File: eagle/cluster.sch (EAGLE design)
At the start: 12 parts, among them J1 B7B-ZR_(LF)(SN)

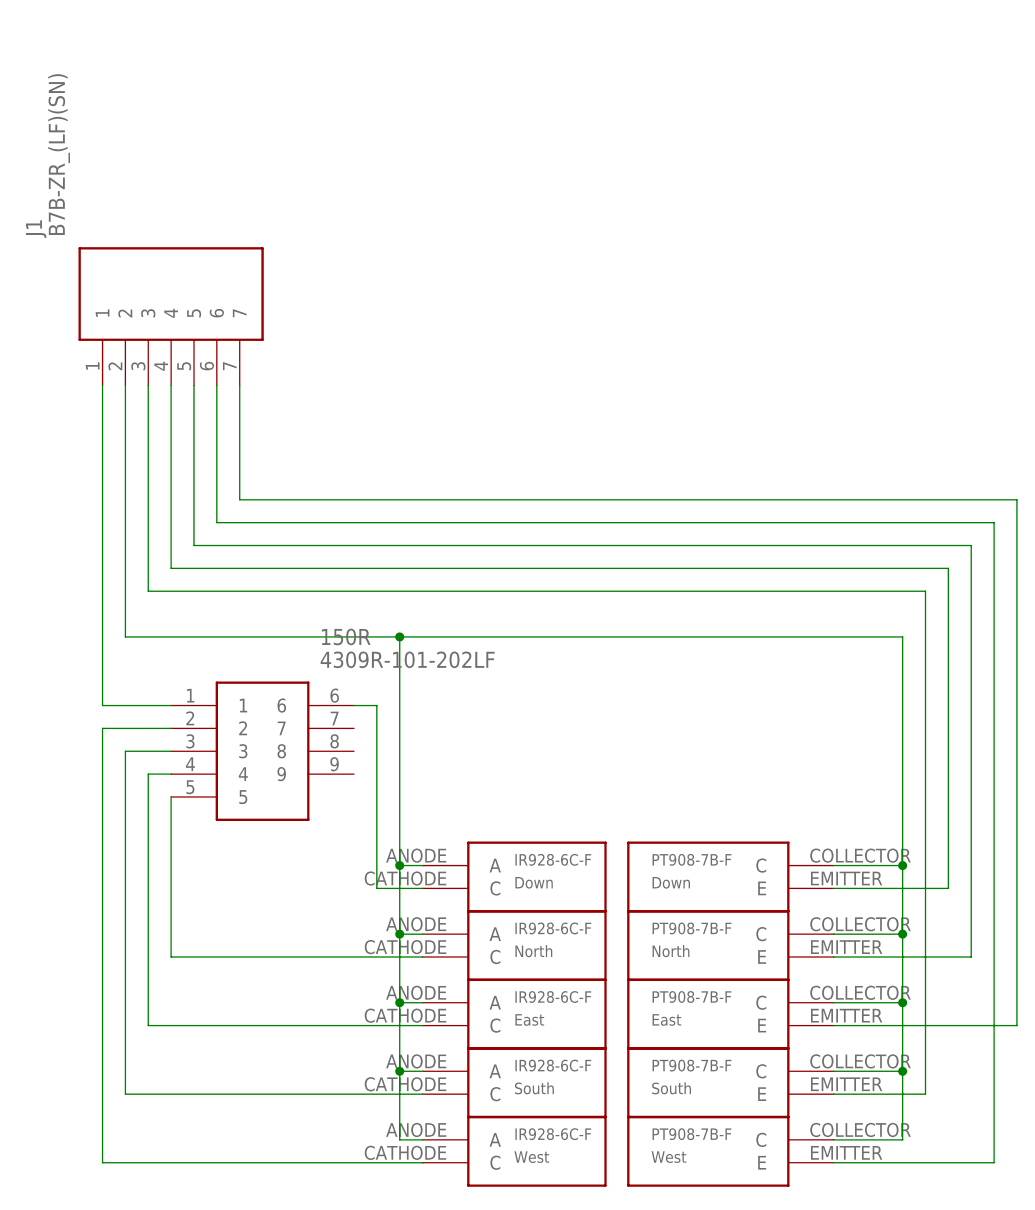
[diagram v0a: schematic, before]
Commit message: Fix drill holes and outer dimensions on cluster and left thumb cluster
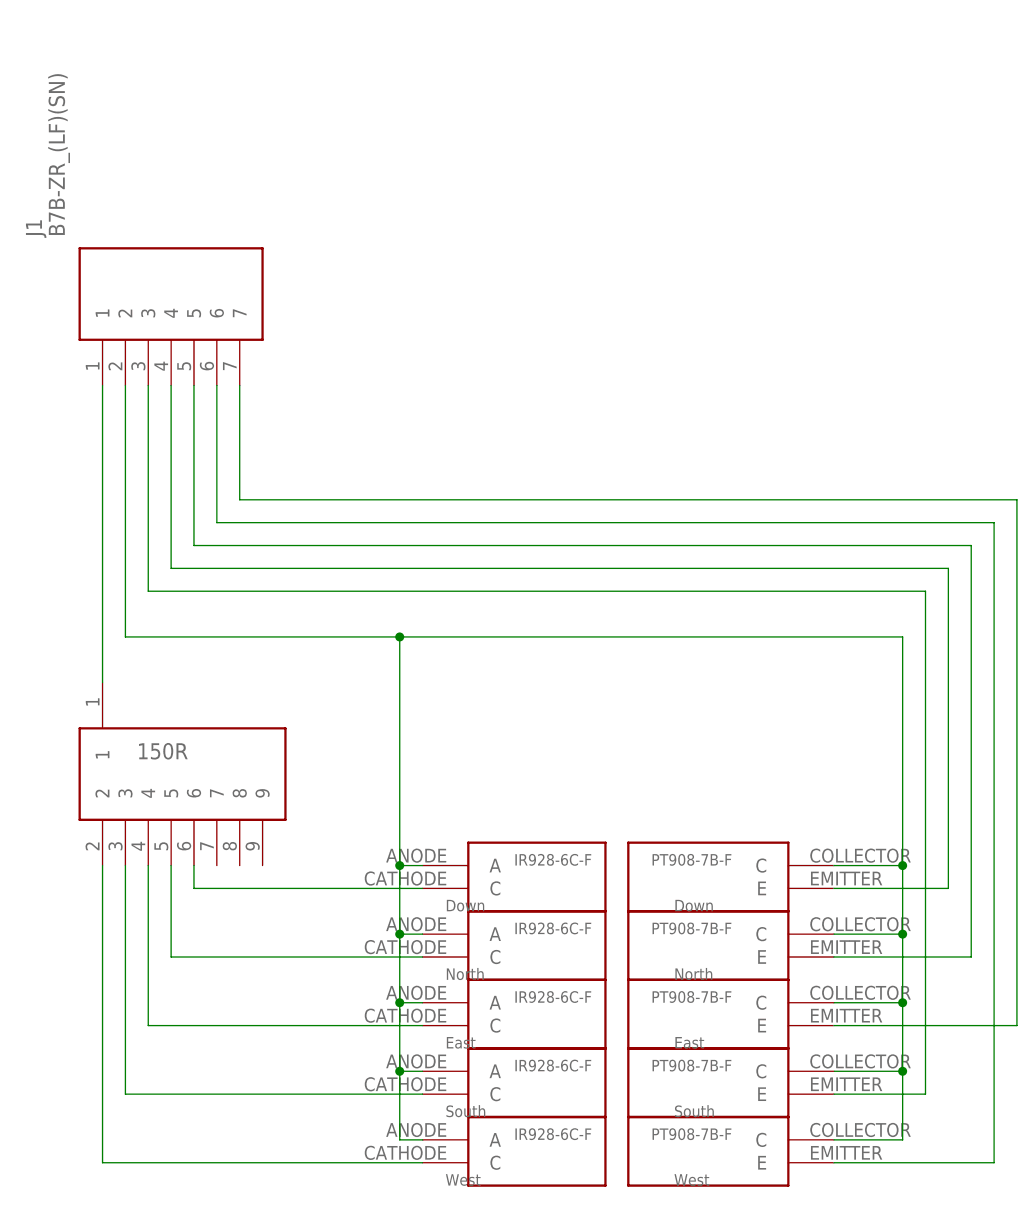
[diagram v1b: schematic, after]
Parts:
- 150R: value 4309R-101-202LF -> 150R; device 4309R-101-202LF:4309R-101-202LF -> 9 pin resistor network:9PIN-RESISTOR-NETWORK9PIN-RESISTOR-NETWORK
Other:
- moved on the sheet: 150R
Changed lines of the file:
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@@
 <?xml version="1.0" encoding="utf-8"?>
 <!DOCTYPE eagle SYSTEM "eagle.dtd">
-<eagle version="9.3.2">
+<eagle version="9.4.2">
 <drawing>
 <settings>
@@
 <part name="LED4" library="IR928-6C-F" deviceset="IR928-6C-F" device="" value="South"/>
 <part name="LED5" library="IR928-6C-F" deviceset="IR928-6C-F" device="" value="West"/>
-<part name="150R" library="4309R-101-202LF" deviceset="4309R-101-202LF" device=""/>
+<part name="150R" library="9 pin resistor network" deviceset="9PIN-RESISTOR-NETWORK" device="9PIN-RESISTOR-NETWORK" value="150R"/>
 </parts>
 <sheets>
@@
 <attribute name="VALUE" x="-86.36" y="173.99" size="1.778" layer="96" rot="R90" align="center-left"/>
 </instance>
-<instance part="PT1" gate="G$1" x="-10.16" y="101.6" smashed="yes">
-<attribute name="VALUE" x="-20.32" y="101.6" size="1.27" layer="96"/>
+<instance part="PT1" gate="G$1" x="0" y="101.6" smashed="yes">
+<attribute name="VALUE" x="-17.78" y="99.06" size="1.27" layer="96"/>
 </instance>
-<instance part="PT2" gate="G$1" x="-10.16" y="93.98" smashed="yes">
-<attribute name="VALUE" x="-20.32" y="93.98" size="1.27" layer="96"/>
+<instance part="PT2" gate="G$1" x="0" y="93.98" smashed="yes">
+<attribute name="VALUE" x="-17.78" y="91.44" size="1.27" layer="96"/>
 </instance>
-<instance part="PT3" gate="G$1" x="-10.16" y="86.36" smashed="yes">
-<attribute name="VALUE" x="-20.32" y="86.36" size="1.27" layer="96"/>
+<instance part="PT3" gate="G$1" x="0" y="86.36" smashed="yes">
+<attribute name="VALUE" x="-17.78" y="83.82" size="1.27" layer="96"/>
 </instance>
-<instance part="PT4" gate="G$1" x="-10.16" y="78.74" smashed="yes">
-<attribute name="VALUE" x="-20.32" y="78.74" size="1.27" layer="96"/>
+<instance part="PT4" gate="G$1" x="0" y="78.74" smashed="yes">
+<attribute name="VALUE" x="-17.78" y="76.2" size="1.27" layer="96"/>
 </instance>
-<instance part="PT5" gate="G$1" x="-10.16" y="71.12" smashed="yes">
-<attribute name="VALUE" x="-20.32" y="71.12" size="1.27" layer="96"/>
+<instance part="PT5" gate="G$1" x="0" y="71.12" smashed="yes">
+<attribute name="VALUE" x="-17.78" y="68.58" size="1.27" layer="96"/>
 </instance>
-<instance part="LED1" gate="G$1" x="-38.1" y="104.14" smashed="yes">
-<attribute name="VALUE" x="-35.56" y="101.6" size="1.27" layer="96"/>
+<instance part="LED1" gate="G$1" x="-45.72" y="101.6" smashed="yes">
+<attribute name="VALUE" x="-43.18" y="99.06" size="1.27" layer="96"/>
 </instance>
-<instance part="LED2" gate="G$1" x="-38.1" y="96.52" smashed="yes">
-<attribute name="VALUE" x="-35.56" y="93.98" size="1.27" layer="96"/>
+<instance part="LED2" gate="G$1" x="-45.72" y="93.98" smashed="yes">
+<attribute name="VALUE" x="-43.18" y="91.44" size="1.27" layer="96"/>
 </instance>
-<instance part="LED3" gate="G$1" x="-38.1" y="88.9" smashed="yes">
-<attribute name="VALUE" x="-35.56" y="86.36" size="1.27" layer="96"/>
+<instance part="LED3" gate="G$1" x="-45.72" y="86.36" smashed="yes">
+<attribute name="VALUE" x="-43.18" y="83.82" size="1.27" layer="96"/>
 </instance>
-<instance part="LED4" gate="G$1" x="-38.1" y="81.28" smashed="yes">
-<attribute name="VALUE" x="-35.56" y="78.74" size="1.27" layer="96"/>
+<instance part="LED4" gate="G$1" x="-45.72" y="78.74" smashed="yes">
+<attribute name="VALUE" x="-43.18" y="76.2" size="1.27" layer="96"/>
 </instance>
-<instance part="LED5" gate="G$1" x="-38.1" y="73.66" smashed="yes">
-<attribute name="VALUE" x="-35.56" y="71.12" size="1.27" layer="96"/>
+<instance part="LED5" gate="G$1" x="-45.72" y="71.12" smashed="yes">
+<attribute name="VALUE" x="-43.18" y="68.58" size="1.27" layer="96"/>
 </instance>
-<instance part="150R" gate="G$1" x="-73.66" y="121.92" smashed="yes">
-<attribute name="NAME" x="-57.15" y="129.54" size="1.778" layer="95" align="center-left"/>
-<attribute name="VALUE" x="-57.15" y="127" size="1.778" layer="96" align="center-left"/>
+<instance part="150R" gate="G$1" x="-81.28" y="124.46" smashed="yes">
+<attribute name="NAME" x="-77.47" y="116.84" size="1.778" layer="95" align="center-left"/>
 </instance>
 </instances>
@@
 <pinref part="J1" gate="G$1" pin="1"/>
 <pinref part="150R" gate="G$1" pin="1"/>
-<wire x1="-81.28" y1="157.48" x2="-81.28" y2="121.92" width="0.1524" layer="91"/>
-<wire x1="-81.28" y1="121.92" x2="-73.66" y2="121.92" width="0.1524" layer="91"/>
+<wire x1="-81.28" y1="157.48" x2="-81.28" y2="124.46" width="0.1524" layer="91"/>
 </segment>
 </net>
@@
 <segment>
 <pinref part="150R" gate="G$1" pin="2"/>
-<wire x1="-73.66" y1="119.38" x2="-81.28" y2="119.38" width="0.1524" layer="91"/>
 <pinref part="LED5" gate="G$1" pin="C"/>
-<wire x1="-81.28" y1="119.38" x2="-81.28" y2="71.12" width="0.1524" layer="91"/>
+<wire x1="-81.28" y1="104.14" x2="-81.28" y2="71.12" width="0.1524" layer="91"/>
 <wire x1="-81.28" y1="71.12" x2="-45.72" y2="71.12" width="0.1524" layer="91"/>
 </segment>
@@
 <segment>
 <pinref part="150R" gate="G$1" pin="3"/>
-<wire x1="-73.66" y1="116.84" x2="-78.74" y2="116.84" width="0.1524" layer="91"/>
 <pinref part="LED4" gate="G$1" pin="C"/>
-<wire x1="-78.74" y1="116.84" x2="-78.74" y2="78.74" width="0.1524" layer="91"/>
+<wire x1="-78.74" y1="104.14" x2="-78.74" y2="78.74" width="0.1524" layer="91"/>
 <wire x1="-78.74" y1="78.74" x2="-45.72" y2="78.74" width="0.1524" layer="91"/>
 </segment>
@@
 <segment>
 <pinref part="150R" gate="G$1" pin="4"/>
-<wire x1="-73.66" y1="114.3" x2="-76.2" y2="114.3" width="0.1524" layer="91"/>
 <pinref part="LED3" gate="G$1" pin="C"/>
-<wire x1="-76.2" y1="114.3" x2="-76.2" y2="86.36" width="0.1524" layer="91"/>
+<wire x1="-76.2" y1="104.14" x2="-76.2" y2="86.36" width="0.1524" layer="91"/>
 <wire x1="-76.2" y1="86.36" x2="-45.72" y2="86.36" width="0.1524" layer="91"/>
 </segment>
@@
 <pinref part="150R" gate="G$1" pin="5"/>
 <pinref part="LED2" gate="G$1" pin="C"/>
-<wire x1="-73.66" y1="111.76" x2="-73.66" y2="93.98" width="0.1524" layer="91"/>
+<wire x1="-73.66" y1="104.14" x2="-73.66" y2="93.98" width="0.1524" layer="91"/>
 <wire x1="-73.66" y1="93.98" x2="-45.72" y2="93.98" width="0.1524" layer="91"/>
 </segment>
@@
 <segment>
 <pinref part="LED1" gate="G$1" pin="C"/>
-<wire x1="-45.72" y1="101.6" x2="-50.8" y2="101.6" width="0.1524" layer="91"/>
 <pinref part="150R" gate="G$1" pin="6"/>
-<wire x1="-53.34" y1="121.92" x2="-50.8" y2="121.92" width="0.1524" layer="91"/>
-<wire x1="-50.8" y1="121.92" x2="-50.8" y2="101.6" width="0.1524" layer="91"/>
+<wire x1="-71.12" y1="104.14" x2="-71.12" y2="101.6" width="0.1524" layer="91"/>
+<wire x1="-71.12" y1="101.6" x2="-45.72" y2="101.6" width="0.1524" layer="91"/>
 </segment>
 </net>
